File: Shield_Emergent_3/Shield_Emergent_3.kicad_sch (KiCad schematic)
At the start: 23 parts, among them J1 Conn_02x06_Counter_Clockwise

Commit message: v0.2 some additions in the circuit
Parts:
- removed D1, D2, D6: LED, LED_SMD:LED_0603_1608Metric_Pad1.05x0.95mm_HandSolder, symbol Device:LED
- removed D4: D_TVS, Diode_SMD:D_SOD-123F, symbol Device:D_TVS
- removed J1: Conn_02x06_Counter_Clockwise, symbol Connector_Generic:Conn_02x06_Counter_Clockwise
- removed R1, R6: 100k, Resistor_SMD:R_0603_1608Metric_Pad0.98x0.95mm_HandSolder, symbol Device:R
- removed R2, R3, R7: 240, Resistor_SMD:R_0603_1608Metric_Pad0.98x0.95mm_HandSolder, symbol Device:R
- added D8: D_TVS, Diode_SMD:D_SOD-123F, symbol Device:D_TVS
- added J2: Conn_01x06, Connector_PinHeader_2.54mm:PinHeader_1x06_P2.54mm_Vertical, symbol Connector_Generic:Conn_01x06
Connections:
- net EN1: now also J2.4 (Pin_4)
- net EN2: now also J2.5 (Pin_5)
- net GND: now also D3.1 (A1), D8.1 (A1), J2.1 (Pin_1); no longer D3.2 (A2)
- net VBUS: now also J2.2 (Pin_2)
- net VOUT1: now also D3.2 (A2); no longer D3.1 (A1)
- net VOUT2: now also D8.2 (A2)
- net nFLT1: now also J2.3 (Pin_3)
- net nFLT2: now also J2.6 (Pin_6)
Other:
- moved on the sheet: C1, C2, C3, C4, D5, D7, R4, R5, R8, R9, U1, U2

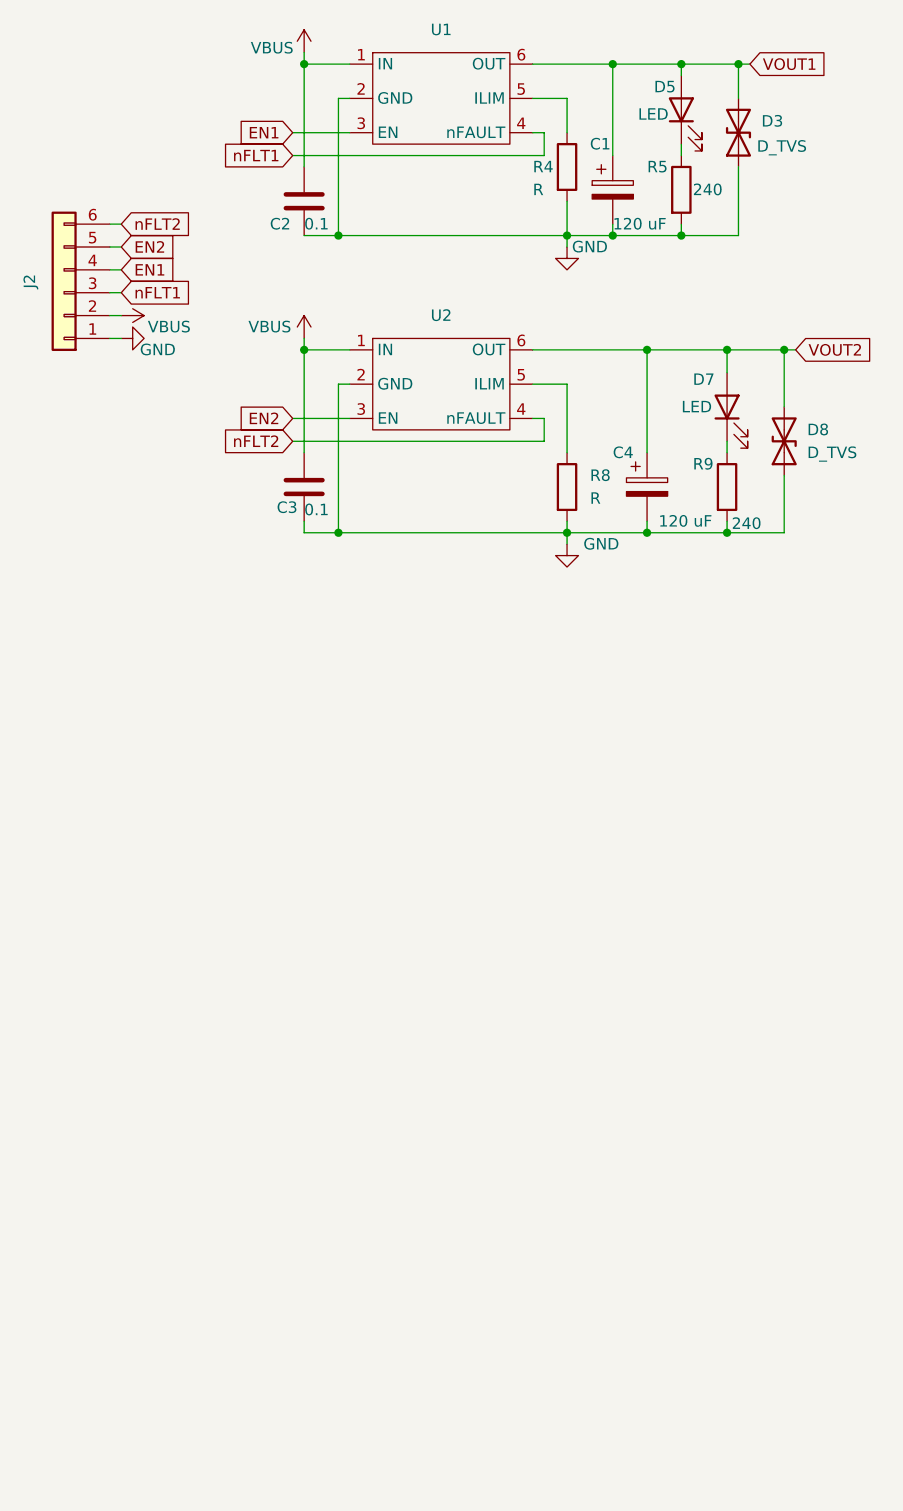
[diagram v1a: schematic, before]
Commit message: v0.3 USB outputs ant TVSs are in circuit
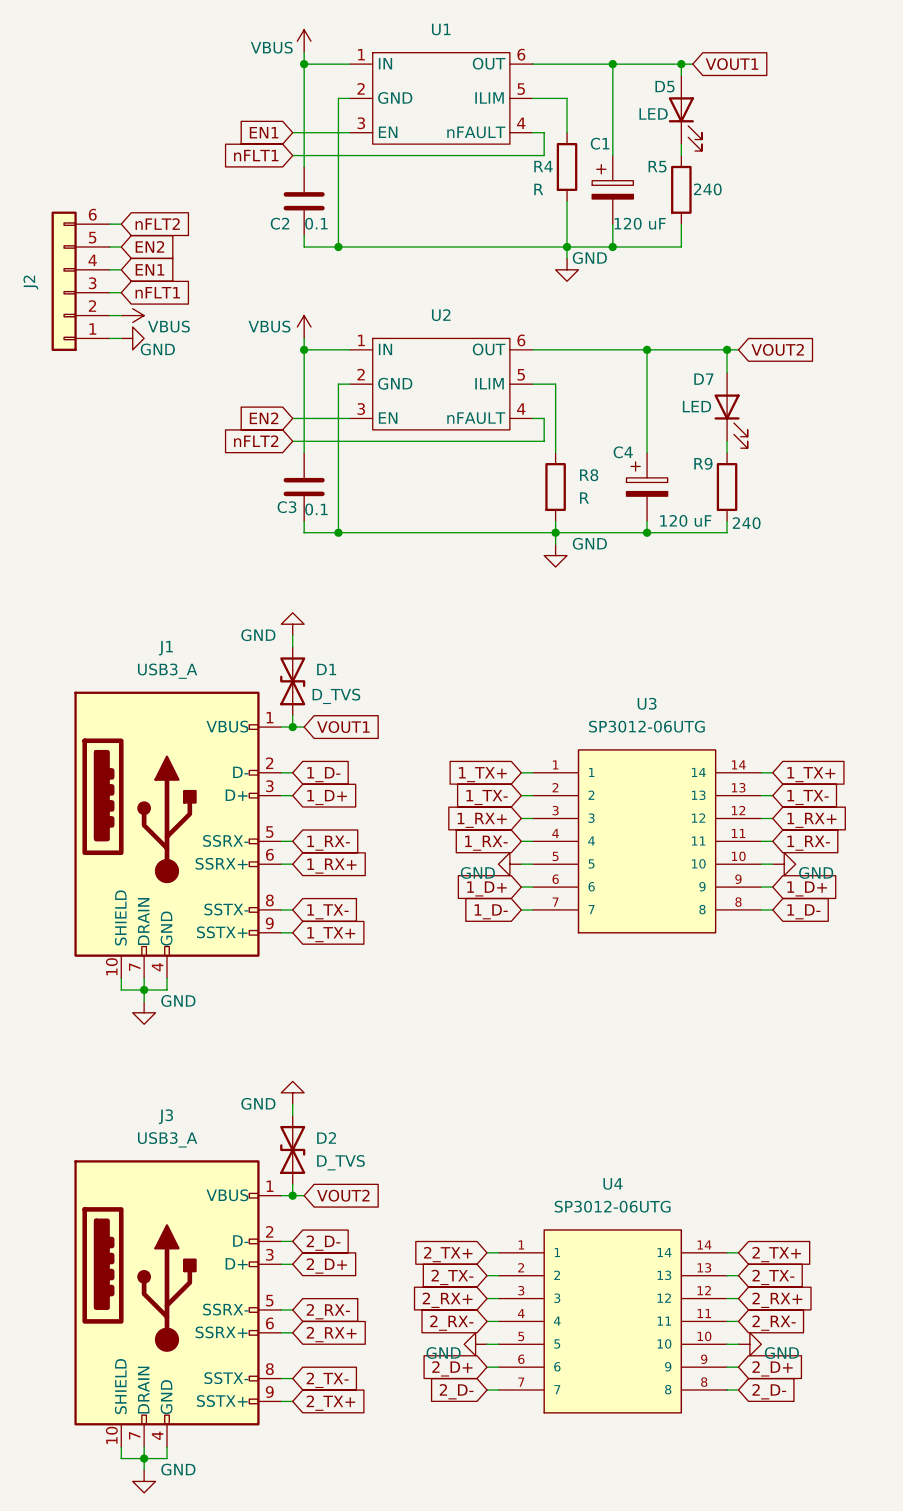
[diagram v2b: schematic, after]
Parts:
- removed D3, D8: D_TVS, Diode_SMD:D_SOD-123F, symbol Device:D_TVS
- added D1, D2: D_TVS, Diode_SMD:D_SOD-123F, symbol Device:D_TVS
- added J1, J3: USB3_A, Connector_USB:USB3_A_Plug_Wuerth_692112030100_Horizontal, symbol Connector:USB3_A
- added U3, U4: SP3012-06UTG, SP3012-06UTG:SON50P350X135X55-14N, symbol myLib8:SP3012-06UTG
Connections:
- net GND: now also D1.2 (A2), D2.2 (A2), J1.10 (SHIELD), J1.4 (GND), J1.7 (DRAIN), J3.10 (SHIELD), J3.4 (GND), J3.7 (DRAIN), U3.10, U3.5, U4.10, U4.5
- net VOUT1: now also D1.1 (A1), J1.1 (VBUS)
- net VOUT2: now also D2.1 (A1), J3.1 (VBUS)
- new net 1_D+: J1.3 (D+), U3.6, U3.9
- new net 1_D-: J1.2 (D-), U3.7, U3.8
- new net 1_RX+: J1.6 (SSRX+), U3.12, U3.3
- new net 1_RX-: J1.5 (SSRX-), U3.11, U3.4
- new net 1_TX+: J1.9 (SSTX+), U3.1, U3.14
- new net 1_TX-: J1.8 (SSTX-), U3.13, U3.2
- new net 2_D+: J3.3 (D+), U4.6, U4.9
- new net 2_D-: J3.2 (D-), U4.7, U4.8
- new net 2_RX+: J3.6 (SSRX+), U4.12, U4.3
- new net 2_RX-: J3.5 (SSRX-), U4.11, U4.4
- new net 2_TX+: J3.9 (SSTX+), U4.1, U4.14
- new net 2_TX-: J3.8 (SSTX-), U4.13, U4.2
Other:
- moved on the sheet: R8

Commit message: v0.4 Circuit was modified. Seems 2B completed
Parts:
- added C5, C6, C7, C8: C, Capacitor_SMD:C_0402_1005Metric, symbol Device:C
- added J10, J11, J12, J13, J14, J15, J16, J19, J20, J4, J5, J7, J8, J9: Conn_01x01_Male, Shield1:smdPin, symbol Connector:Conn_01x01_Male
- added J17, J18, J6: Conn_01x01_Male, Shield1:throughPin, symbol Connector:Conn_01x01_Male
- added X1: USB_C_24pins, Shield1:FPC_12, symbol Shield1:USB_C_24pins
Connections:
- net 1_D+: no longer J1.3 (D+)
- net 1_D-: no longer J1.2 (D-)
- net GND: now also C5.1, C6.1, J18.1 (Pin_1), J19.1 (Pin_1), J20.1 (Pin_1), X1.A1 (GND), X1.A12 (GND), X1.B1 (GND), X1.B12 (GND), X1.S1 (SHIELD), X1.S2 (SHIELD), X1.S3 (SHIELD), X1.S4 (SHIELD)
- net VBUS: now also C5.2, C6.2, C7.2, C8.2, J4.1 (Pin_1), J5.1 (Pin_1), X1.A4 (VBUS), X1.A9 (VBUS), X1.B4 (VBUS), X1.B9 (VBUS)
- net 1_RX+ renamed RX1+
- net RX1+: now also J10.1 (Pin_1), X1.B11 (RX1+)
- net 1_RX- renamed RX1-
- net RX1-: now also J9.1 (Pin_1), X1.B10 (RX1-)
- net 1_TX+ renamed TX1+
- net TX1+: now also J12.1 (Pin_1), X1.A2 (TX1+)
- net 1_TX- renamed TX1-
- net TX1-: now also J11.1 (Pin_1), X1.A3 (TX1-)
- net 2_RX+ renamed RX2+
- net RX2+: now also J14.1 (Pin_1), X1.A11 (RX2+)
- net 2_RX- renamed RX2-
- net RX2-: now also J13.1 (Pin_1), X1.A10 (RX2-)
- net 2_TX+ renamed TX2+
- net TX2+: now also J16.1 (Pin_1), X1.B2 (TX2+)
- net 2_TX- renamed TX2-
- net TX2-: now also J15.1 (Pin_1), X1.B3 (TX2-)
- new net D+: J1.3 (D+), J8.1 (Pin_1), X1.A6 (D+), X1.B6 (D+)
- new net D-: J1.2 (D-), J7.1 (Pin_1), X1.A7 (D-), X1.B7 (D-)
- new net GND2: C7.1, C8.1
- new net RX: J6.1 (Pin_1), X1.A5 (CC1), X1.B5 (CC2)
- new net TX: J17.1 (Pin_1), X1.A8 (SBU1), X1.B8 (SBU2)
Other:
- moved on the sheet: D1, D2, J1, J3, U3, U4

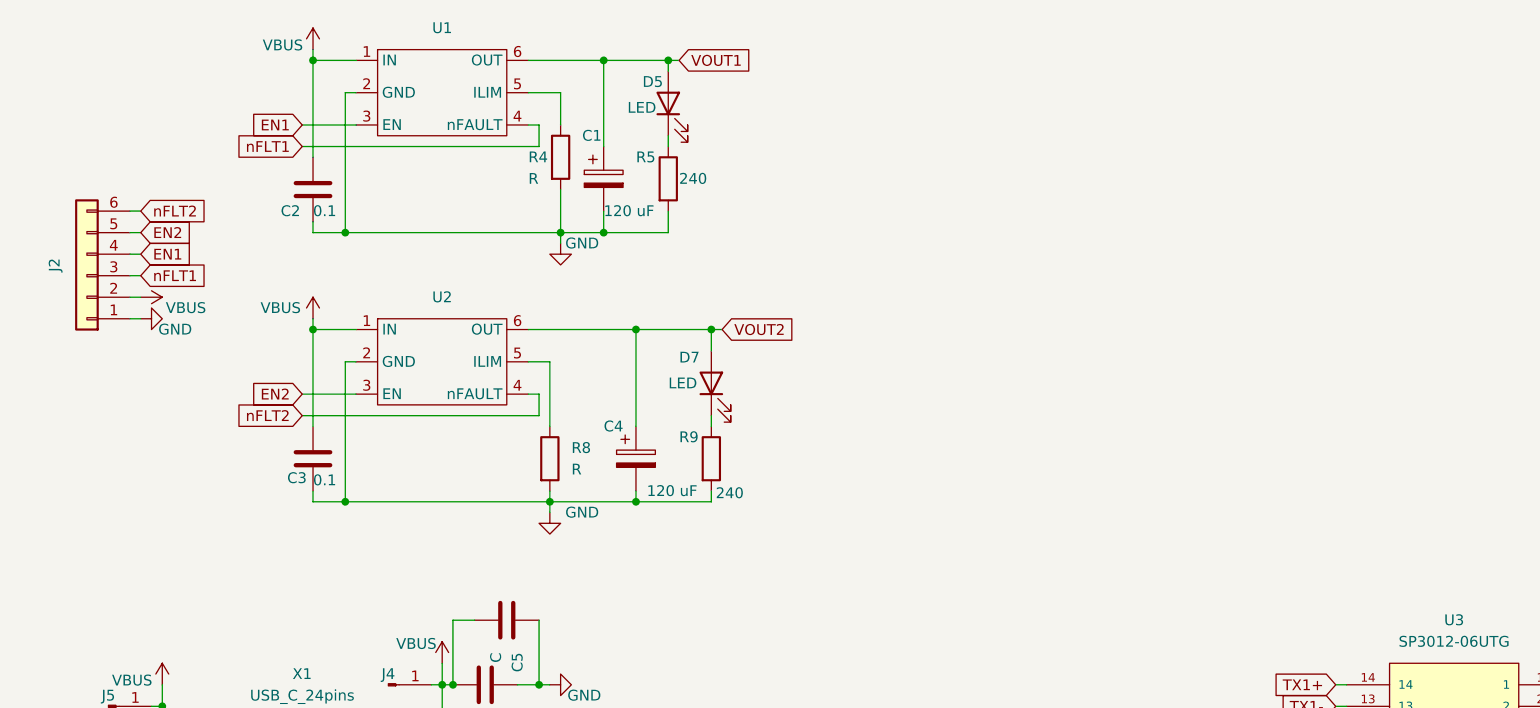
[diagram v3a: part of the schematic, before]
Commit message: v0.5 Management connector was added
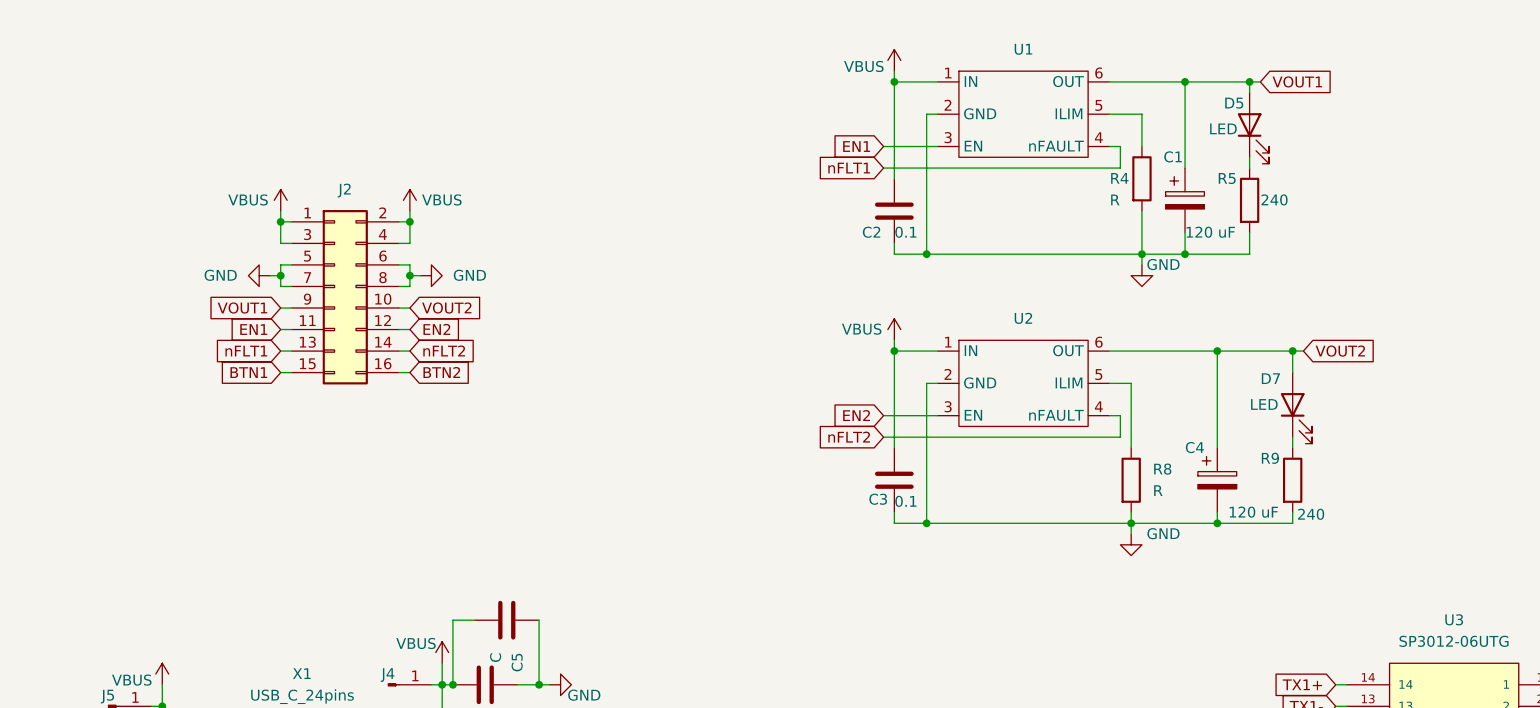
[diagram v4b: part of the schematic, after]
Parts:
- removed J2: Conn_01x06, Connector_PinHeader_2.54mm:PinHeader_1x06_P2.54mm_Vertical, symbol Connector_Generic:Conn_01x06
- added J2: Conn_02x08_Odd_Even, Connector_PinSocket_2.54mm:PinSocket_2x08_P2.54mm_Vertical, symbol Connector_Generic:Conn_02x08_Odd_Even
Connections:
- net EN1: now also J2.11 (Pin_11)
- net EN2: now also J2.12 (Pin_12)
- net GND: now also J2.5 (Pin_5), J2.6 (Pin_6), J2.7 (Pin_7), J2.8 (Pin_8)
- net VBUS: now also J2.1 (Pin_1), J2.2 (Pin_2), J2.3 (Pin_3), J2.4 (Pin_4)
- net VOUT1: now also J2.9 (Pin_9)
- net VOUT2: now also J2.10 (Pin_10)
- net nFLT1: now also J2.13 (Pin_13)
- net nFLT2: now also J2.14 (Pin_14)
- new net BTN1: J2.15 (Pin_15)
- new net BTN2: J2.16 (Pin_16)
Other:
- moved on the sheet: C1, C2, C3, C4, D5, D7, R4, R5, R8, R9, U1, U2

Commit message: v0.6 draft circuit, draft decomposition
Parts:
- removed C5, C6, C7, C8: C, Capacitor_SMD:C_0402_1005Metric, symbol Device:C
- removed D5, D7: LED, LED_SMD:LED_0603_1608Metric_Pad1.05x0.95mm_HandSolder, symbol Device:LED
- removed J1, J3: USB3_A, Connector_USB:USB3_A_Plug_Wuerth_692112030100_Horizontal, symbol Connector:USB3_A
- removed J10, J11, J12, J13, J14, J15, J16, J19, J20, J4, J5, J7, J8, J9: Conn_01x01_Male, Shield1:smdPin, symbol Connector:Conn_01x01_Male
- removed J17, J18, J6: Conn_01x01_Male, Shield1:throughPin, symbol Connector:Conn_01x01_Male
- removed R5, R9: 240, Resistor_SMD:R_0603_1608Metric_Pad0.98x0.95mm_HandSolder, symbol Device:R
- added J1, J3: USB3_B_Micro, USB_Conns:MU3MS04, symbol Connector:USB3_B_Micro
- added R1: 0, Resistor_SMD:R_0402_1005Metric, symbol Device:R
- U3, U4: footprint SP3012-06UTG:SON50P350X135X55-14N -> Package_DFN_QFN:DFN-14_1.35x3.5mm_P0.5mm
- X1: footprint Shield1:FPC_12 -> Connector_USB:USB_C_Receptacle_JAE_DX07S024WJ3R400
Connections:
- net 1_D+ is gone; now on net D+: U3.6, U3.9
- net 1_D- is gone; now on net D-: U3.7, U3.8
- net 2_D+: now also J3.3 (D+)
- net 2_D-: now also J3.2 (D-)
- net D+: now also J1.3 (D+)
- net D-: now also J1.2 (D-)
- net GND: now also J1.11 (SHIELD), J1.5 (GND), J1.8 (DRAIN), J3.11 (SHIELD), J3.5 (GND), J3.8 (DRAIN), R1.2; no longer X1.S1 (SHIELD), X1.S2 (SHIELD), X1.S3 (SHIELD), X1.S4 (SHIELD)
- net RX1+: now also J1.10 (SSRX+)
- net RX1-: now also J1.9 (SSRX-)
- net RX2+: now also J3.10 (SSRX+)
- net RX2-: now also J3.9 (SSRX-)
- net TX1+: now also J1.7 (SSTX+)
- net TX1-: now also J1.6 (SSTX-)
- net TX2+: now also J3.7 (SSTX+)
- net TX2-: now also J3.6 (SSTX-)
- net VOUT1: now also J1.1 (VBUS)
- net VOUT2: now also J3.1 (VBUS)
- net RX: no longer names the net of X1.A5 (CC1)
- net RX: no longer X1.B5 (CC2)
- net TX: no longer names the net of X1.A8 (SBU1)
- net TX: no longer X1.B8 (SBU2)
- new net Shield: R1.1, X1.S1 (SHIELD), X1.S2 (SHIELD), X1.S3 (SHIELD), X1.S4 (SHIELD)
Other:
- moved on the sheet: D1, D2, J2, U3, U4, X1

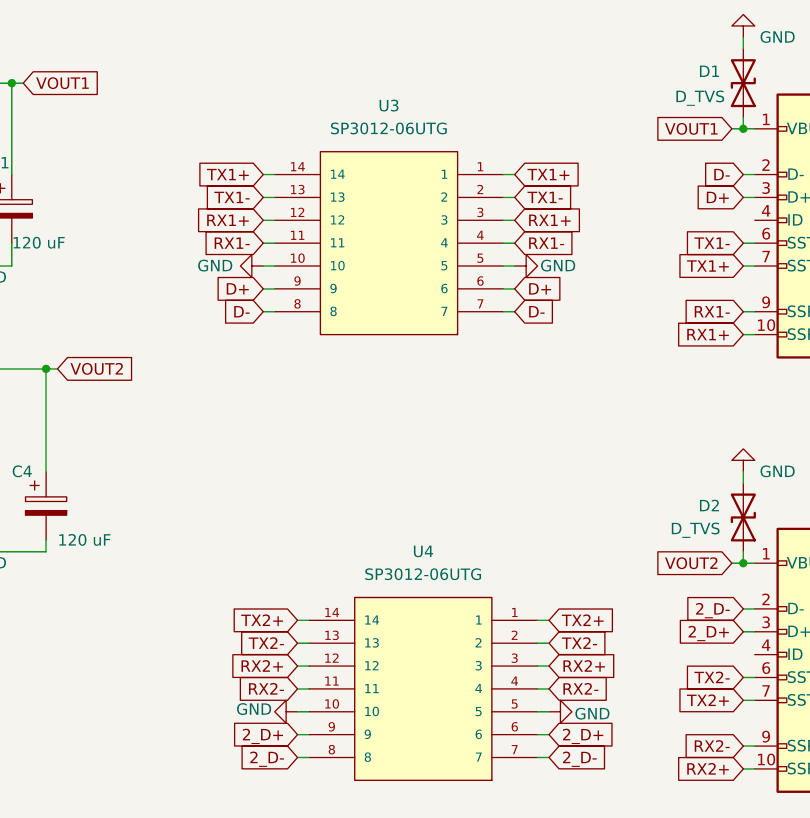
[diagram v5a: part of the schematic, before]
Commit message: v0.7 nets were modified footprints were corrected Rdy 4 decomposition.
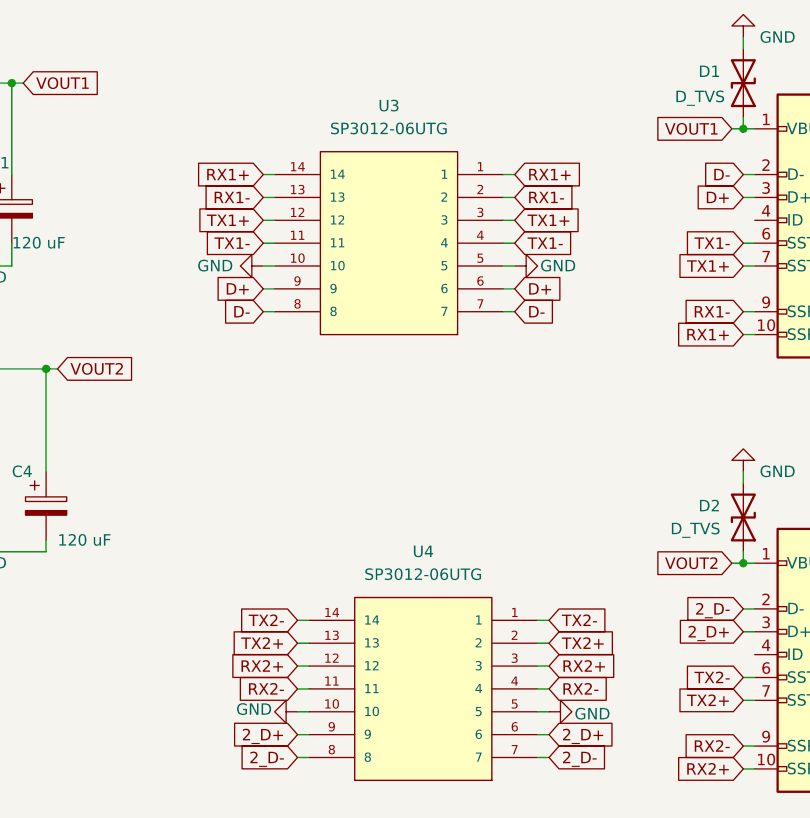
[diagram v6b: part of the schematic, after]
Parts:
- U3, U4: footprint Package_DFN_QFN:DFN-14_1.35x3.5mm_P0.5mm -> myLib8:DFN-14_1.35x3.5mm_P0.5mm
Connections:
- net RX1+: now also U3.1, U3.14; no longer U3.12, U3.3
- net RX1-: now also U3.13, U3.2; no longer U3.11, U3.4
- net TX1+: now also U3.12, U3.3; no longer U3.1, U3.14
- net TX1-: now also U3.11, U3.4; no longer U3.13, U3.2
- net TX2+: now also U4.13, U4.2; no longer U4.1, U4.14
- net TX2-: now also U4.1, U4.14; no longer U4.13, U4.2
